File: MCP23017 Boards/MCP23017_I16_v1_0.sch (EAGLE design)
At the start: 59 parts, among them IC3 74HC540N, IC4 74HC540N, IC5 MCP23017SP, X4 057-016-0

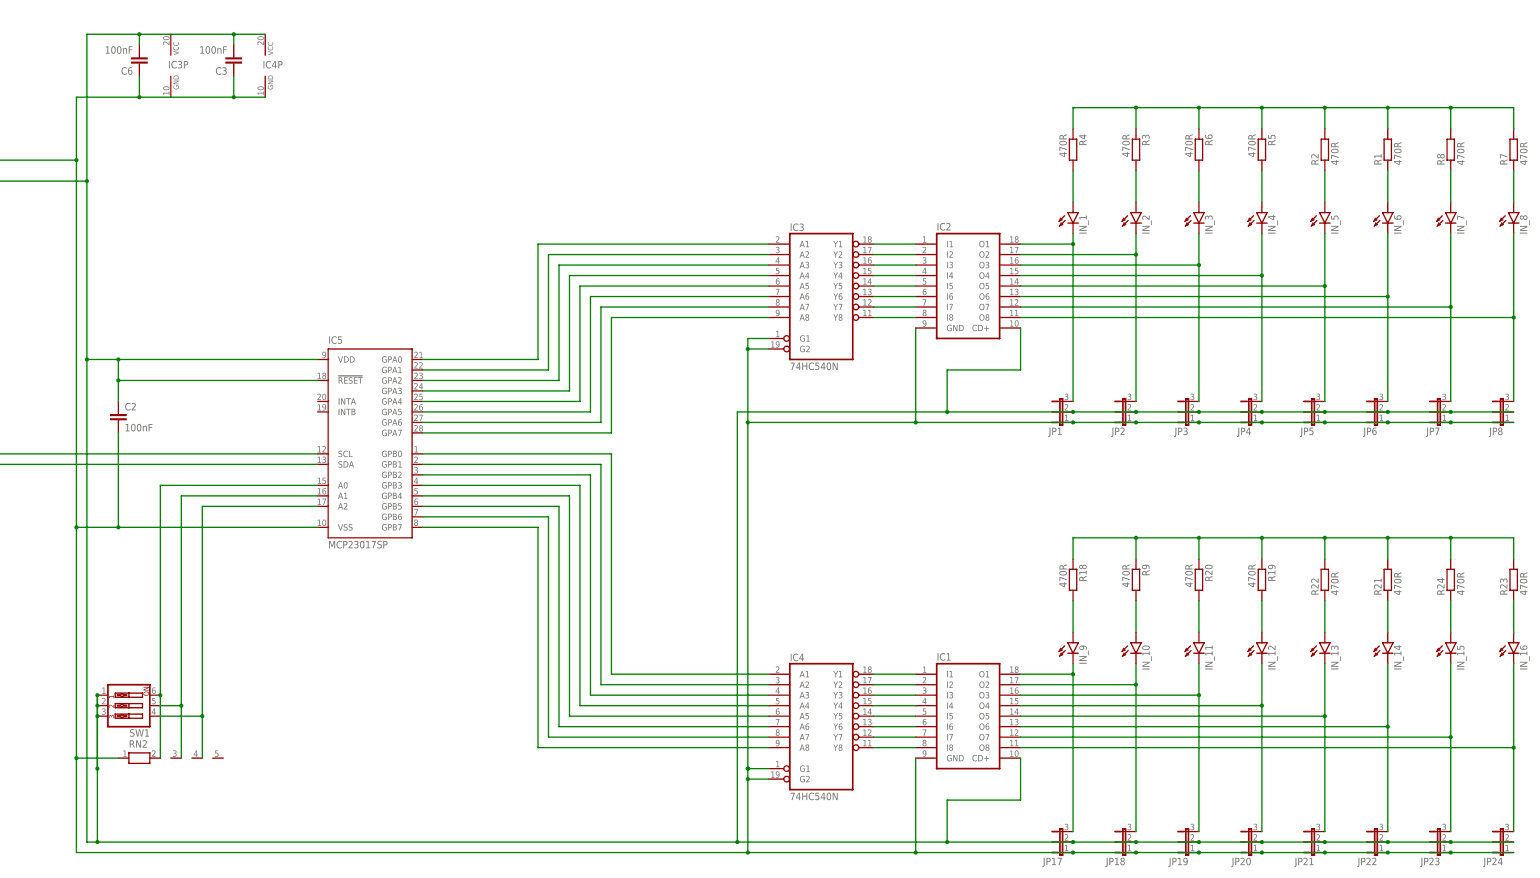
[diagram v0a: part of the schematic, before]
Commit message: Update MCP23017_I16_v1_0.sch
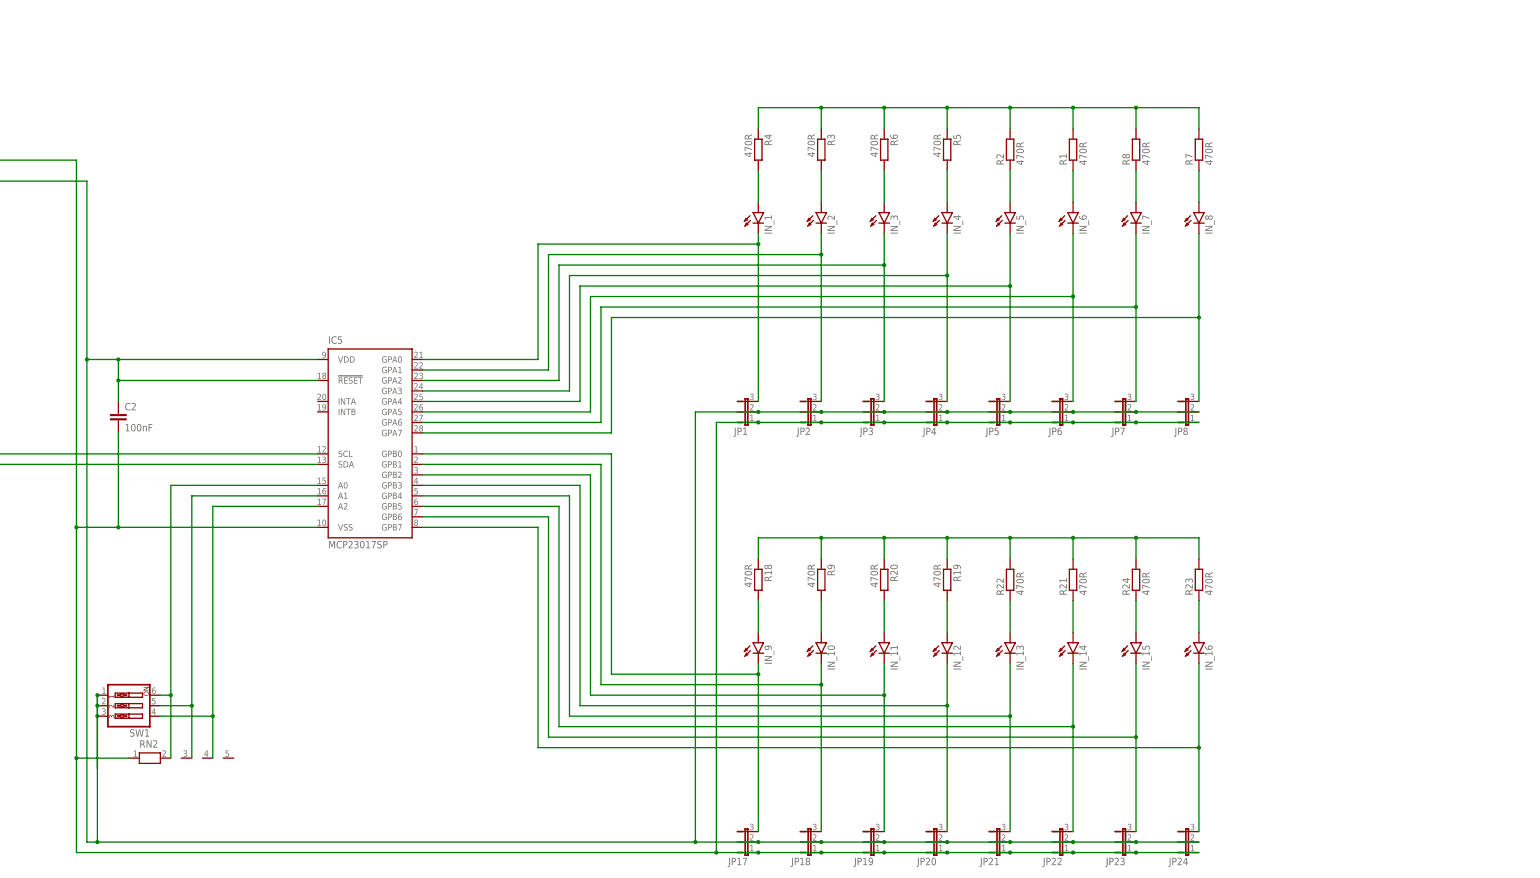
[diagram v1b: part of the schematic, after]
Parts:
- removed C3, C6: 100nF, resistor:C-EU025-024X044
- removed IC1, IC2: (no value), uln-udn:ULN2803A
- removed IC3, IC4: 74HC540N, 74xx-eu:74HC540N
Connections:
- removed net N$12: IC2.I8, IC3A.Y8
- removed net N$14: IC2.I7, IC3A.Y7
- removed net N$15: IC2.I6, IC3A.Y6
- removed net N$16: IC2.I5, IC3A.Y5
- removed net N$17: IC2.I4, IC3A.Y4
- removed net N$18: IC2.I3, IC3A.Y3
- removed net N$19: IC2.I2, IC3A.Y2
- removed net N$2 (its old number): IC2.O2, IN_2.C, JP2.3
- removed net N$20: IC2.I1, IC3A.Y1
- removed net N$21: IC3A.A1, IC5.GPA0
- removed net N$23: IC3A.A3, IC5.GPA2
- removed net N$25: IC3A.A5, IC5.GPA4
- removed net N$27: IC3A.A7, IC5.GPA6
- removed net N$34: IC1.I8, IC4A.Y8
- removed net N$37: IC1.O2, IN_10.C, JP18.3
- removed net N$39: IC1.I7, IC4A.Y7
- removed net N$4: IC2.O4, IN_4.C, JP4.3
- removed net N$40: IC1.I6, IC4A.Y6
- removed net N$41: IC1.O4, IN_12.C, JP20.3
- removed net N$43: IC1.O6, IN_14.C, JP22.3
- removed net N$44: IC1.I5, IC4A.Y5
- removed net N$45: IC1.I4, IC4A.Y4
- removed net N$46: IC1.I3, IC4A.Y3
- removed net N$47: IC1.I2, IC4A.Y2
- removed net N$48: IC1.I1, IC4A.Y1
- removed net N$49: IC4A.A1, IC5.GPB0
- removed net N$51: IC4A.A3, IC5.GPB2
- removed net N$54: IC1.O8, IN_16.C, JP24.3
- removed net N$55: IC4A.A5, IC5.GPB4
- removed net N$57: IC4A.A7, IC5.GPB6
- removed net N$7: IC2.O6, IN_6.C, JP6.3
- removed net N$9: IC2.O8, IN_8.C, JP8.3
- net GND1: no longer C3.1, C6.1, IC1.GND, IC2.GND, IC3A.G1, IC3A.G2, IC3P.GND, IC4A.G1, IC4A.G2, IC4P.GND
- net N$1: now also IC5.GPA0; no longer IC2.O1
- net N$22: now also IN_2.C, JP2.3; no longer IC3A.A2
- net N$24: now also IN_4.C, JP4.3; no longer IC3A.A4
- net N$26: now also IN_6.C, JP6.3; no longer IC3A.A6
- net N$28: now also IN_8.C, JP8.3; no longer IC3A.A8
- net N$3: now also IC5.GPA2; no longer IC2.O3
- net N$36: now also IC5.GPB0; no longer IC1.O1
- net N$38: now also IC5.GPB2; no longer IC1.O3
- net N$42: now also IC5.GPB4; no longer IC1.O5
- net N$5: now also IC5.GPA4; no longer IC2.O5
- net N$50: now also IN_10.C, JP18.3; no longer IC4A.A2
- net N$52: now also IN_12.C, JP20.3; no longer IC4A.A4
- net N$53: now also IC5.GPB6; no longer IC1.O7
- net N$56: now also IN_14.C, JP22.3; no longer IC4A.A6
- net N$58: now also IN_16.C, JP24.3; no longer IC4A.A8
- net N$8: now also IC5.GPA6; no longer IC2.O7
- net VCC5.2: no longer C3.2, C6.2, IC1.CD+, IC2.CD+, IC3P.VCC, IC4P.VCC
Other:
- moved on the sheet: IN_1, IN_10, IN_11, IN_12, IN_13, IN_14, IN_15, IN_16, IN_2, IN_3, IN_4, IN_5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

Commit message: Update MCP23017_I16_v1_0.sch
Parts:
- RN2: device resistor-net:RN04 -> resistor-net_edit:RN03
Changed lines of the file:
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@@
 <part name="C2" library="resistor" library_urn="urn:adsk.eagle:library:348" deviceset="C-EU" device="025-024X044" package3d_urn="urn:adsk.eagle:package:23630/1" value="100nF"/>
 <part name="SW1" library="special" library_urn="urn:adsk.eagle:library:367" deviceset="SW_DIP-3" device="" package3d_urn="urn:adsk.eagle:package:26663/2"/>
-<part name="RN2" library="resistor-net" library_urn="urn:adsk.eagle:library:343" deviceset="RN04" device="" package3d_urn="urn:adsk.eagle:package:24976/1"/>
+<part name="RN2" library="resistor-net_edit" deviceset="RN03" device=""/>
 <part name="IC5" library="microchip-6" deviceset="MCP23017" device="SP"/>
 <part name="R3" library="resistor" library_urn="urn:adsk.eagle:library:348" deviceset="R-EU_" device="0309/10" package3d_urn="urn:adsk.eagle:package:23567/1" value="470R"/>
@@
 <attribute name="VALUE" x="78.74" y="-48.26" size="1.778" layer="96" rot="R180"/>
 </instance>
-<instance part="RN2" gate="1" x="78.74" y="-68.58" smashed="yes">
+<instance part="RN2" gate="G$1" x="78.74" y="-68.58" smashed="yes">
 <attribute name="NAME" x="76.2" y="-66.04" size="1.778" layer="95"/>
 <attribute name="VALUE" x="76.2" y="-72.898" size="1.778" layer="96"/>
@@
 <pinref part="SW1" gate="A" pin="4"/>
 <wire x1="81.28" y1="-58.42" x2="93.98" y2="-58.42" width="0.1524" layer="91"/>
-<pinref part="RN2" gate="1" pin="4"/>
+<pinref part="RN2" gate="G$1" pin="4"/>
 <wire x1="93.98" y1="-68.58" x2="93.98" y2="-58.42" width="0.1524" layer="91"/>
 <junction x="93.98" y="-58.42"/>
@@
 <pinref part="SW1" gate="A" pin="5"/>
 <wire x1="81.28" y1="-55.88" x2="88.9" y2="-55.88" width="0.1524" layer="91"/>
-<pinref part="RN2" gate="1" pin="3"/>
+<pinref part="RN2" gate="G$1" pin="3"/>
 <wire x1="88.9" y1="-68.58" x2="88.9" y2="-55.88" width="0.1524" layer="91"/>
 <junction x="88.9" y="-55.88"/>
@@
 <wire x1="33.02" y1="76.2" x2="60.96" y2="76.2" width="0.1524" layer="91"/>
 <junction x="33.02" y="83.82"/>
-<pinref part="RN2" gate="1" pin="1"/>
+<pinref part="RN2" gate="G$1" pin="1"/>
 <wire x1="215.9" y1="-91.44" x2="215.9" y2="12.7" width="0.1524" layer="91"/>
 <wire x1="73.66" y1="-68.58" x2="60.96" y2="-68.58" width="0.1524" layer="91"/>
@@
 <net name="N$2" class="0">
 <segment>
-<pinref part="RN2" gate="1" pin="2"/>
+<pinref part="RN2" gate="G$1" pin="2"/>
 <wire x1="83.82" y1="-68.58" x2="83.82" y2="-53.34" width="0.1524" layer="91"/>
 <pinref part="SW1" gate="A" pin="6"/>
